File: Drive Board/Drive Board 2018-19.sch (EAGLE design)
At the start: 68 parts, among them IC1 ACS758KCB, IC2 ACS758KCB, IC3 ACS758KCB, IC4 ACS758KCB, IC5 7812T, K1 JTN-PCB-DC6V

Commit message: Started board routing
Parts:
- removed K1: JTN-PCB-DC6V, relay:JTN-PCB-DC6V
- added MINISRV1, MINISRV10, MINISRV11, MINISRV2, MINISRV3, MINISRV4, MINISRV5, MINISRV6, MINISRV7, MINISRV8, MINISRV9: MINI-FIT-SR-R, Molex:MINI-FIT-SR-R
- added U$11: JTN1AS-PA-F-DC12V, RSX_driver_relay:JTN1AS-PA-F-DC12V
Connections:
- removed net N$14: IC3.IP-
- removed net N$15: IC2.IP-
- removed net N$20: IC1.IP-
- removed net N$23: IC4.IP-
- removed net N$38: B2.*D3, U$6.P$5
- removed net N$39: B2.*D5, U$5.P$5
- removed net N$40: B2.*D6, U$4.P$5
- removed net N$41: B2.*D9, U$3.P$5
- removed net N$42: B2.*D10, U$2.P$5
- removed net N$43: B2.*D11, U$1.P$5
- removed net N$44: B2.D0, U$6.P$4
- removed net N$45: B2.D1, U$5.P$4
- removed net N$46: B2.D2, U$4.P$4
- removed net N$47: B2.D4, U$3.P$4
- removed net N$48: B2.D7, U$2.P$4
- removed net N$49: B2.D8, U$1.P$4
- removed net N$57: U$5.P$1
- removed net N$63: U$3.P$1
- new net D0: B2.D0, U$1.P$4
- new net D1: B2.D1, U$2.P$4
- new net D10: B2.*D10, U$5.P$5
- new net D11: B2.*D11, U$6.P$5
- new net D12: B2.D12
- new net D13: B2.D13
- new net D2: B2.D2, U$3.P$4
- new net D3: B2.*D3, U$1.P$5
- new net D4: B2.D4, U$4.P$4
- new net D5: B2.*D5, U$2.P$5
- new net D6: B2.*D6, U$3.P$5
- new net D7: B2.D7, U$5.P$4
- new net D8: B2.D8, U$6.P$4
- new net D9: B2.*D9, U$4.P$5
- new net N$35: R18.2, U$5.P$1
- new net N$37: R20.2, U$3.P$1
- new net N$59: SV1.4
- new net OUT1: IC1.IP-, MINISRV10.PS2
- new net OUT2: IC2.IP-, MINISRV9.PS2
- new net OUT3: IC4.IP-, MINISRV7.PS2
- new net OUT4: IC3.IP-, MINISRV8.PS2
- new net OUTA1: MINISRV1.PS2, U$1.OUTA1, U$1.OUTA2
- new net OUTA2: MINISRV2.PS2, U$2.OUTA1, U$2.OUTA2
- new net OUTA3: MINISRV3.PS2, U$3.OUTA1, U$3.OUTA2
- new net OUTA4: MINISRV4.PS2, U$4.OUTA1, U$4.OUTA2
- new net OUTA5: MINISRV5.PS2, U$5.OUTA1, U$5.OUTA2
- new net OUTA6: MINISRV6.PS2, U$6.OUTA1, U$6.OUTA2
- new net OUTB1: MINISRV1.PS1, U$1.OUTB1, U$1.OUTB2
- new net OUTB2: MINISRV2.PS1, U$2.OUTB1, U$2.OUTB2
- new net OUTB3: MINISRV3.PS1, U$3.OUTB1, U$3.OUTB2
- new net OUTB4: MINISRV4.PS1, U$4.OUTB1, U$4.OUTB2
- new net OUTB5: MINISRV5.PS1, U$5.OUTB1, U$5.OUTB2
- new net OUTB6: MINISRV6.PS1, U$6.OUTB1, U$6.OUTB2
- net 3V3: now also S8.1
- net ARDUINO_GND: now also R22.1; no longer SV1.4
- net BATTERY_V+: now also MINISRV11.PS1, MINISRV11.PS2, U$11.VIN
- net BATTERY_V-: now also MINISRV10.PS1, MINISRV7.PS1, MINISRV8.PS1, MINISRV9.PS1
- net N$18: now also U$11.NO; no longer K1G$2.O
- net N$22: now also B2.GND@1; no longer B2.GND@2
- net N$36: now also U$11.COIL_V_+; no longer K1G$1.2
- net N$7: now also U$11.COIL_V_-\; no longer K1G$1.1
- net N$72: now also R12.2
- net N$73: now also R11.2
- net N$74: now also R10.2
- net N$75: now also R9.2
- net N$76: now also R13.2
- net N$77: now also R16.2
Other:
- moved on the sheet: LED2, LED3, LED4, LED5, LED6, LED7, R10, R11, R12, R13, R16, R9

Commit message: first attempt finished for board design
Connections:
- net N$18 renamed CURR_SENSE
- removed net N$22: B2.GND@1, X4.1, X4.2
- removed net N$59: SV1.4
- new net ESTOP: C7.1, IC5.VI, MINISRV11.PS2
- net ARDUINO_GND: now also B2.GND@1, SV1.4, X4.1, X4.2
- net BATTERY_V+: no longer C7.1, IC5.VI, MINISRV11.PS2
- net D0: now also U$6.P$4; no longer U$1.P$4
- net D1: now also U$5.P$4; no longer U$2.P$4
- net D10: now also U$2.P$5; no longer U$5.P$5
- net D11: now also U$1.P$5; no longer U$6.P$5
- net D2: now also U$4.P$4; no longer U$3.P$4
- net D3: now also U$6.P$5; no longer U$1.P$5
- net D4: now also U$3.P$4; no longer U$4.P$4
- net D5: now also U$5.P$5; no longer U$2.P$5
- net D6: now also U$4.P$5; no longer U$3.P$5
- net D7: now also U$2.P$4; no longer U$5.P$4
- net D8: now also U$1.P$4; no longer U$6.P$4
- net D9: now also U$3.P$5; no longer U$4.P$5

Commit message: Re doing layout, just need planes
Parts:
- removed MINISRV1, MINISRV10, MINISRV2, MINISRV3, MINISRV4, MINISRV5, MINISRV6, MINISRV7, MINISRV8, MINISRV9: MINI-FIT-SR-R, Molex:MINI-FIT-SR-R
- removed U$10, U$8: BUSBAR_MOUNT, RSX_Busbar_contact:BUSBAR_MOUNT
- added K1, K2, K3: G5L, relay:G5L
- added U$12, U$13: MEGA-FIT_RA_12, RSX:MEGA-FIT_RA_12
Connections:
- removed net CURR_SENSE: IC1.IP+, IC2.IP+, IC3.IP+, IC4.IP+, U$11.NO
- removed net N$36: C8.1, D1.C, IC5.VO, OK1.EMIT, R4.2, U$11.COIL_V_+
- removed net N$7: D1.A, LED1.C, Q1.E, U$11.COIL_V_-\
- new net COIL_V+: C8.1, D1.C, IC5.VO, K11.2, K21.2, K31.2, OK1.EMIT, R4.2, U$11.COIL_V_+
- new net COIL_V-: D1.A, K11.1, K21.1, K31.1, LED1.C, Q1.E, U$11.COIL_V_-\
- new net IC1_IN: IC1.IP+, K32.S
- new net IC2_IN: IC2.IP+, K22.S
- new net IC3_IN: IC3.IP+, K12.S
- new net N$24: IC4.IP+, U$11.NO
- net BATTERY_V+: now also K12.P, K22.P, K32.P, MINISRV11.PS2; no longer MINISRV11.PS1, U$8.CONTACT
- net BATTERY_V-: now also U$13.P$1, U$13.P$2, U$13.P$3, U$13.P$4, U$13.P$5, U$13.P$6; no longer MINISRV10.PS1, MINISRV7.PS1, MINISRV8.PS1, MINISRV9.PS1, U$10.CONTACT
- net D0: now also U$1.P$4; no longer U$6.P$4
- net D1: now also U$2.P$4; no longer U$5.P$4
- net D10: now also U$5.P$5; no longer U$2.P$5
- net D11: now also U$6.P$5; no longer U$1.P$5
- net D2: now also U$3.P$4; no longer U$4.P$4
- net D3: now also U$1.P$5; no longer U$6.P$5
- net D4: now also U$4.P$4; no longer U$3.P$4
- net D5: now also U$2.P$5; no longer U$5.P$5
- net D6: now also U$3.P$5; no longer U$4.P$5
- net D7: now also U$5.P$4; no longer U$2.P$4
- net D8: now also U$6.P$4; no longer U$1.P$4
- net D9: now also U$4.P$5; no longer U$3.P$5
- net ESTOP: now also MINISRV11.PS1; no longer MINISRV11.PS2
- net N$13: now also B2.A1; no longer B2.A2
- net N$19: now also B2.A0; no longer B2.A3
- net N$4: now also B2.A3; no longer B2.A0
- net N$52: now also SV1.1; no longer SV1.2
- net N$53: now also SV1.2; no longer SV1.1
- net N$8: now also B2.A2; no longer B2.A1
- net OUT1: now also U$13.P$12; no longer MINISRV10.PS2
- net OUT2: now also U$13.P$11; no longer MINISRV9.PS2
- net OUT3: now also IC3.IP-, U$13.P$8; no longer IC4.IP-, MINISRV7.PS2
- net OUT4: now also IC4.IP-, U$13.P$7; no longer IC3.IP-, MINISRV8.PS2
- net OUTA1: now also U$12.P$1; no longer MINISRV1.PS2
- net OUTA2: now also U$12.P$2; no longer MINISRV2.PS2
- net OUTA3: now also U$12.P$3; no longer MINISRV3.PS2
- net OUTA4: now also U$12.P$4; no longer MINISRV4.PS2
- net OUTA5: now also U$12.P$5; no longer MINISRV5.PS2
- net OUTA6: now also U$12.P$6; no longer MINISRV6.PS2
- net OUTB1: now also U$12.P$7; no longer MINISRV1.PS1
- net OUTB2: now also U$12.P$8; no longer MINISRV2.PS1
- net OUTB3: now also U$12.P$9; no longer MINISRV3.PS1
- net OUTB4: now also U$12.P$10; no longer MINISRV4.PS1
- net OUTB5: now also U$12.P$11; no longer MINISRV5.PS1
- net OUTB6: now also U$12.P$12; no longer MINISRV6.PS1
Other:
- moved on the sheet: SV1

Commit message: Finished First draft
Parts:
- added IC6: LM741P, linear:LM741P
- added R23: 7.5k, resistor:R-US_0207/10
- added R24: 24k, resistor:R-US_0207/10
- R14, R15: device adafruit:R-US_0309/12 -> resistor:R-US_0207/10
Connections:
- removed net ARDUINO_GND: B2.GND, B2.GND@1, C1.-, C10.-, C2.-, C3.-, C4.-, C5.-, C6.-, C9.-, IC1.GND, IC2.GND, IC3.GND, IC4.GND, LED2.C, LED3.C, LED4.C, LED5.C, LED6.C, LED7.C, R17.1, R18.1, R19.1, R20.1, R21.1, R22.1, R8.1, SV1.4, U$1.P$2, U$1.P$3, U$2.P$2, U$2.P$3, U$3.P$2, U$3.P$3, U$4.P$2, U$4.P$3, U$5.P$2, U$5.P$3, U$6.P$2, U$6.P$3, X4.1, X4.2
- new net A5: B2.A5, IC6.-IN, IC6.OUT
- new net GND: B2.GND, B2.GND@1, C1.-, C10.-, C2.-, C3.-, C4.-, C5.-, C6.-, C9.-, IC1.GND, IC2.GND, IC3.GND, IC4.GND, IC6.V-, LED2.C, LED3.C, LED4.C, LED5.C, LED6.C, LED7.C, R17.1, R18.1, R19.1, R20.1, R21.1, R22.1, R23.2, R8.1, SV1.4, U$1.GND1, U$1.GND2, U$1.P$2, U$1.P$3, U$13.P$1, U$13.P$2, U$13.P$3, U$13.P$4, U$13.P$5, U$13.P$6, U$2.GND1, U$2.GND2, U$2.P$2, U$2.P$3, U$3.GND1, U$3.GND2, U$3.P$2, U$3.P$3, U$4.GND1, U$4.GND2, U$4.P$2, U$4.P$3, U$5.GND1, U$5.GND2, U$5.P$2, U$5.P$3, U$6.GND1, U$6.GND2, U$6.P$2, U$6.P$3, U$9.CONTACT, X4.1, X4.2
- new net N$5: IC6.+IN, R23.1, R24.2
- net 5V: now also IC6.V+, R14.1, R15.1; no longer R14.2, R15.2
- net BATTERY_V+: now also MINISRV11.PS1, R24.1; no longer MINISRV11.PS2
- net BATTERY_V-: no longer U$1.GND1, U$1.GND2, U$13.P$1, U$13.P$2, U$13.P$3, U$13.P$4, U$13.P$5, U$13.P$6, U$2.GND1, U$2.GND2, U$3.GND1, U$3.GND2, U$4.GND1, U$4.GND2, U$5.GND1, U$5.GND2, U$6.GND1, U$6.GND2, U$9.CONTACT
- net ESTOP: now also MINISRV11.PS2; no longer MINISRV11.PS1
- net N$52: now also R15.2; no longer R15.1
- net N$53: now also R14.2; no longer R14.1
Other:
- moved on the sheet: R14, R15

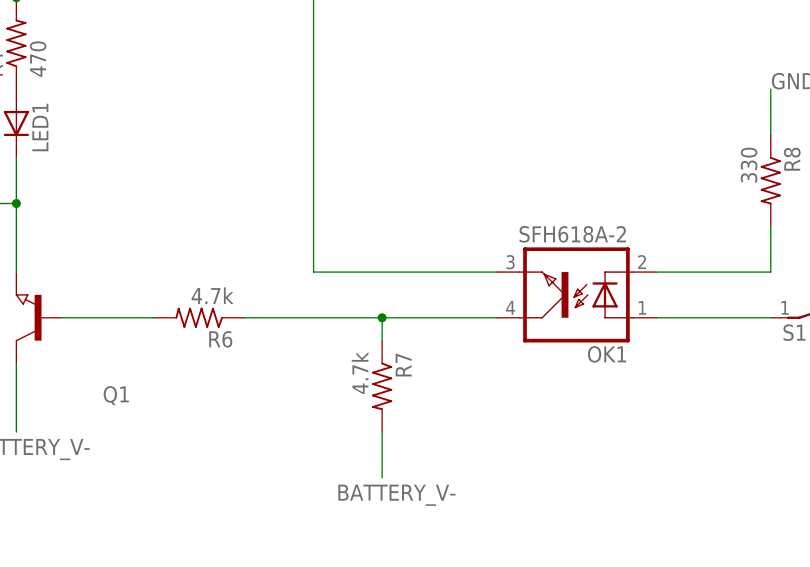
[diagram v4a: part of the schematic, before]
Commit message: Fixed optocoupler mismatched pins
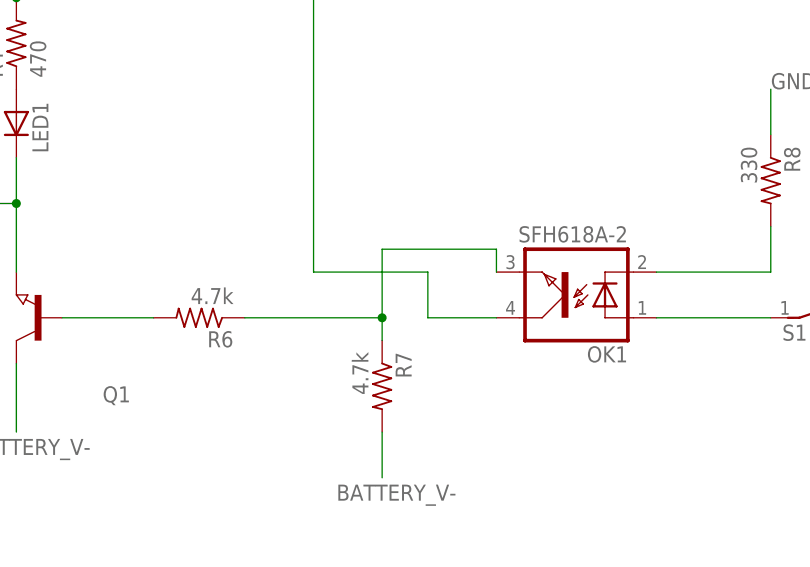
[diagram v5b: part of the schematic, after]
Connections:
- net COIL_V+: now also OK1.COL; no longer OK1.EMIT
- net N$21: now also OK1.EMIT; no longer OK1.COL
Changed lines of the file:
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@@
 <wire x1="-187.96" y1="139.7" x2="-172.72" y2="139.7" width="0.1524" layer="91"/>
 <wire x1="-172.72" y1="139.7" x2="-172.72" y2="137.16" width="0.1524" layer="91"/>
-<wire x1="-160.02" y1="139.7" x2="-172.72" y2="139.7" width="0.1524" layer="91"/>
+<wire x1="-172.72" y1="139.7" x2="-172.72" y2="147.32" width="0.1524" layer="91"/>
 <junction x="-172.72" y="139.7"/>
-<pinref part="OK1" gate="G$1" pin="COL"/>
+<wire x1="-172.72" y1="147.32" x2="-160.02" y2="147.32" width="0.1524" layer="91"/>
+<pinref part="OK1" gate="G$1" pin="EMIT"/>
+<wire x1="-160.02" y1="147.32" x2="-160.02" y2="144.78" width="0.1524" layer="91"/>
 </segment>
 </net>
@@
 <wire x1="-213.36" y1="175.26" x2="-180.34" y2="175.26" width="0.1524" layer="91"/>
 <wire x1="-180.34" y1="175.26" x2="-180.34" y2="144.78" width="0.1524" layer="91"/>
-<pinref part="OK1" gate="G$1" pin="EMIT"/>
-<wire x1="-180.34" y1="144.78" x2="-160.02" y2="144.78" width="0.1524" layer="91"/>
 <pinref part="U$11" gate="G$1" pin="COIL_V_+"/>
 <wire x1="-243.84" y1="175.26" x2="-243.84" y2="172.72" width="0.1524" layer="91"/>
 <wire x1="-243.84" y1="172.72" x2="-254" y2="172.72" width="0.1524" layer="91"/>
+<wire x1="-180.34" y1="144.78" x2="-167.64" y2="144.78" width="0.1524" layer="91"/>
+<wire x1="-167.64" y1="144.78" x2="-167.64" y2="139.7" width="0.1524" layer="91"/>
+<pinref part="OK1" gate="G$1" pin="COL"/>
+<wire x1="-167.64" y1="139.7" x2="-160.02" y2="139.7" width="0.1524" layer="91"/>
 </segment>
 <segment>

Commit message: Update from chris meeting
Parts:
- removed S1: (no value), switch-dil:DS01E
- removed X4: (no value), con-molex-micro-fit-3_0:HEADER_POS4_43045-0401
- added LED8: (no value), eagle-ltspice:LED_E
- added R25: 100k, resistor:R-US_0207/10
- added R26: 500, resistor:R-US_0207/10
- added U$8: JTN1AS-PA-F-DC12V, RSX_driver_relay:JTN1AS-PA-F-DC12V
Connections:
- removed net N$29: B2.5V, S1.2
- removed net N$31: OK1.A, S1.1
- removed net N$33: B2.VIN, X4.4
- new net N$1: LED8.A, R26.1
- net 5V: now also B2.5V, R25.2; no longer X4.3
- net BATTERY_V+: now also U$8.VIN; no longer U$1.VIN1, U$1.VIN2, U$2.VIN1, U$2.VIN2, U$3.VIN1, U$3.VIN2, U$4.VIN1, U$4.VIN2, U$5.VIN1, U$5.VIN2, U$6.VIN1, U$6.VIN2
- net COIL_V+: now also B2.VIN, U$8.COIL_V_+
- net COIL_V-: now also U$8.COIL_V_-\
- net D12: now also OK1.A, R25.1, R26.2
- net GND: now also LED8.C; no longer X4.1, X4.2
- net N$24: now also U$8.NO
- net OUT2: now also U$13.P$10; no longer U$13.P$11
- net OUT4: now also U$1.VIN1, U$1.VIN2, U$2.VIN1, U$2.VIN2, U$3.VIN1, U$3.VIN2, U$4.VIN1, U$4.VIN2, U$5.VIN1, U$5.VIN2, U$6.VIN1, U$6.VIN2; no longer U$13.P$7
- net OUTA1: now also U$12.P$3; no longer U$12.P$1
- net OUTA3: now also U$12.P$1; no longer U$12.P$3
- net OUTA4: now also U$12.P$6; no longer U$12.P$4
- net OUTA6: now also U$12.P$4; no longer U$12.P$6

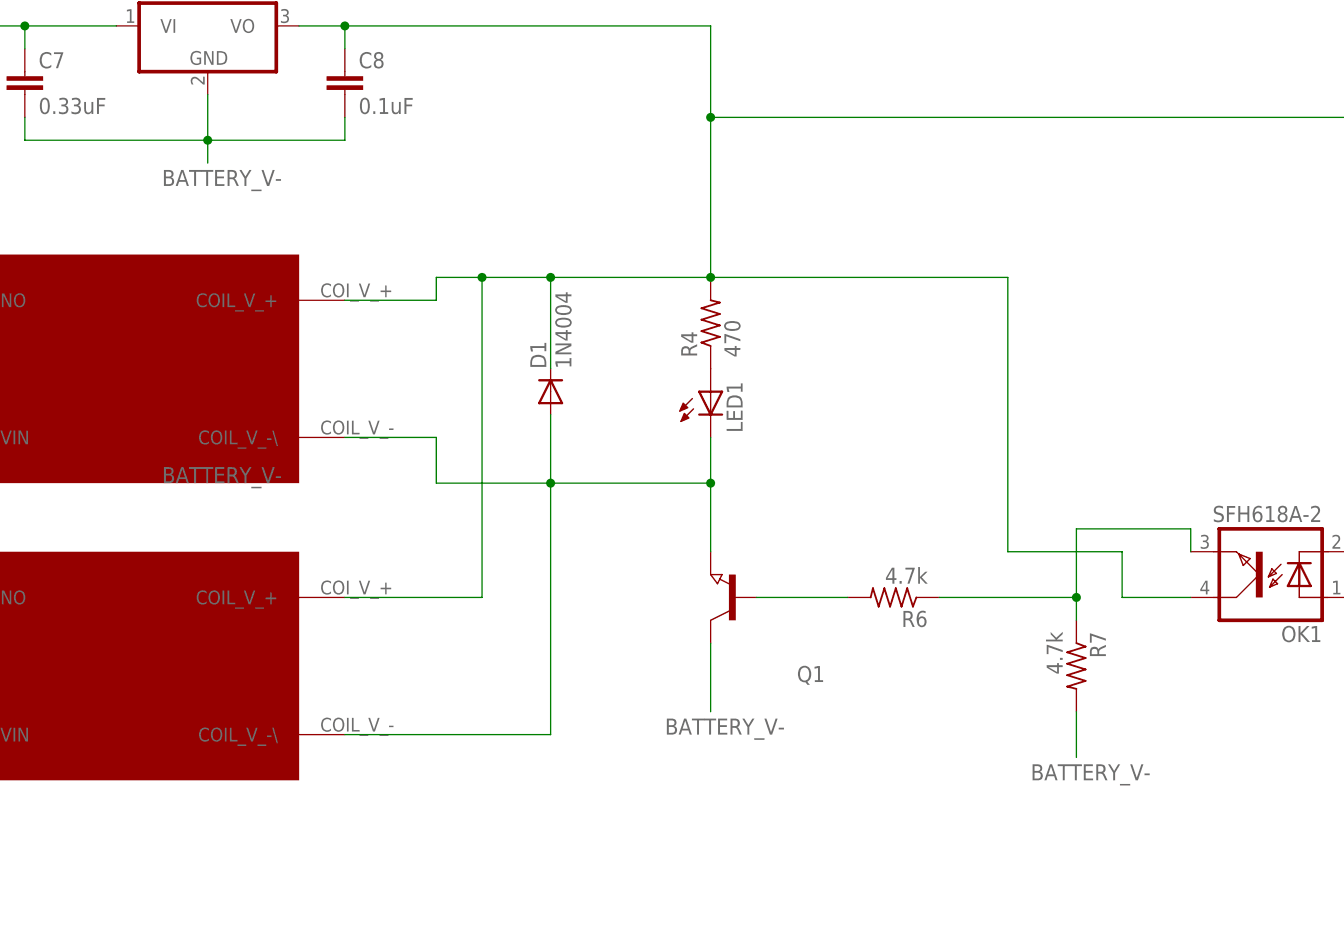
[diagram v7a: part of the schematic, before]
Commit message: Fixed mixed ground signals
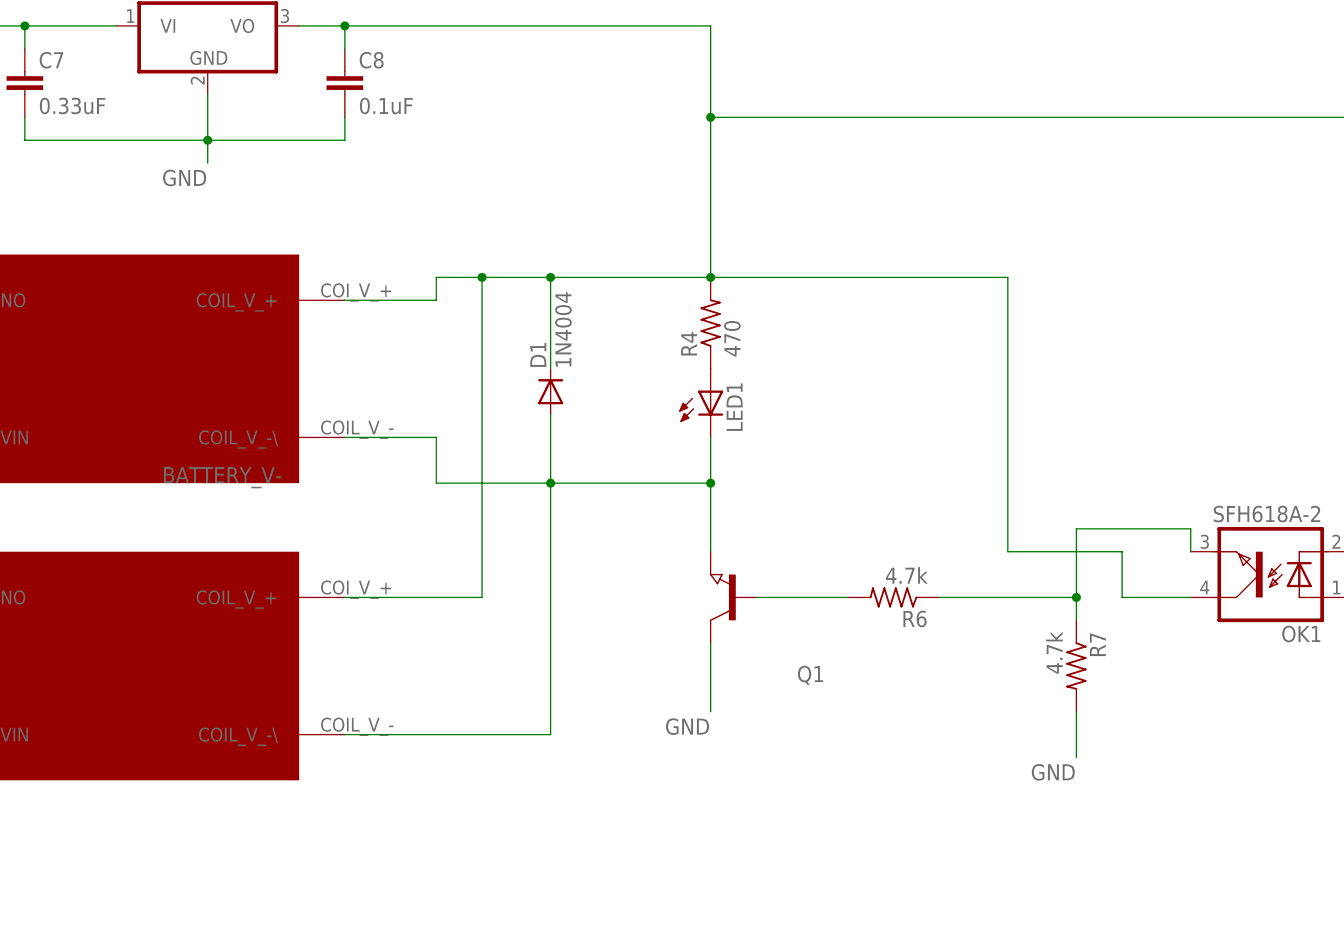
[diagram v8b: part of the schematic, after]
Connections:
- removed net BATTERY_V-: C7.2, C8.2, IC5.GND, Q1.C, R7.2
- net GND: now also C7.2, C8.2, IC5.GND, Q1.C, R7.2
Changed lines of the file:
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@@
 <net name="BATTERY_V-" class="0">
-<segment>
-<pinref part="Q1" gate="G$1" pin="C"/>
-<wire x1="-213.36" y1="134.62" x2="-213.36" y2="127" width="0.1524" layer="91"/>
-<label x="-218.44" y="124.46" size="1.778" layer="95"/>
-</segment>
-<segment>
-<pinref part="R7" gate="G$1" pin="2"/>
-<wire x1="-172.72" y1="127" x2="-172.72" y2="121.92" width="0.1524" layer="91"/>
-<label x="-177.8" y="119.38" size="1.778" layer="95"/>
-</segment>
-<segment>
-<pinref part="IC5" gate="A1" pin="GND"/>
-<wire x1="-269.24" y1="195.58" x2="-269.24" y2="190.5" width="0.1524" layer="91"/>
-<pinref part="C7" gate="G$1" pin="2"/>
-<wire x1="-269.24" y1="190.5" x2="-289.56" y2="190.5" width="0.1524" layer="91"/>
-<wire x1="-289.56" y1="190.5" x2="-289.56" y2="193.04" width="0.1524" layer="91"/>
-<pinref part="C8" gate="G$1" pin="2"/>
-<wire x1="-269.24" y1="190.5" x2="-254" y2="190.5" width="0.1524" layer="91"/>
-<wire x1="-254" y1="190.5" x2="-254" y2="193.04" width="0.1524" layer="91"/>
-<junction x="-269.24" y="190.5"/>
-<wire x1="-269.24" y1="190.5" x2="-269.24" y2="187.96" width="0.1524" layer="91"/>
-<label x="-274.32" y="185.42" size="1.778" layer="95"/>
-</segment>
 <segment>
 <label x="-274.32" y="152.4" size="1.778" layer="95"/>
@@
 <label x="-137.16" y="114.3" size="1.778" layer="95" rot="R270"/>
 </segment>
-</net>
+<segment>
+<pinref part="Q1" gate="G$1" pin="C"/>
+<wire x1="-213.36" y1="134.62" x2="-213.36" y2="127" width="0.1524" layer="91"/>
+<label x="-218.44" y="124.46" size="1.778" layer="95"/>
+</segment>
+<segment>
+<pinref part="R7" gate="G$1" pin="2"/>
+<wire x1="-172.72" y1="127" x2="-172.72" y2="121.92" width="0.1524" layer="91"/>
+<label x="-177.8" y="119.38" size="1.778" layer="95"/>
+</segment>
+<segment>
+<pinref part="IC5" gate="A1" pin="GND"/>
+<wire x1="-269.24" y1="195.58" x2="-269.24" y2="190.5" width="0.1524" layer="91"/>
+<pinref part="C7" gate="G$1" pin="2"/>
+<wire x1="-269.24" y1="190.5" x2="-289.56" y2="190.5" width="0.1524" layer="91"/>
+<wire x1="-289.56" y1="190.5" x2="-289.56" y2="193.04" width="0.1524" layer="91"/>
+<pinref part="C8" gate="G$1" pin="2"/>
+<wire x1="-269.24" y1="190.5" x2="-254" y2="190.5" width="0.1524" layer="91"/>
+<wire x1="-254" y1="190.5" x2="-254" y2="193.04" width="0.1524" layer="91"/>
+<junction x="-269.24" y="190.5"/>
+<wire x1="-269.24" y1="190.5" x2="-269.24" y2="187.96" width="0.1524" layer="91"/>
+<label x="-274.32" y="185.42" size="1.778" layer="95"/>
+</segment>
+</net>
